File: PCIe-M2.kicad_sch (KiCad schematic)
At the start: 24 parts, among them J4 Bus_M.2_Socket_M, M1 M.2 Screw, M2 M.2 Solder Nut, M3 M.2 Solder Nut, M4 M.2 Solder Nut, M5 M.2 Solder Nut, U7 ASEK-32.768KHZ-L-R-T, U8 AP3441SHE-7B

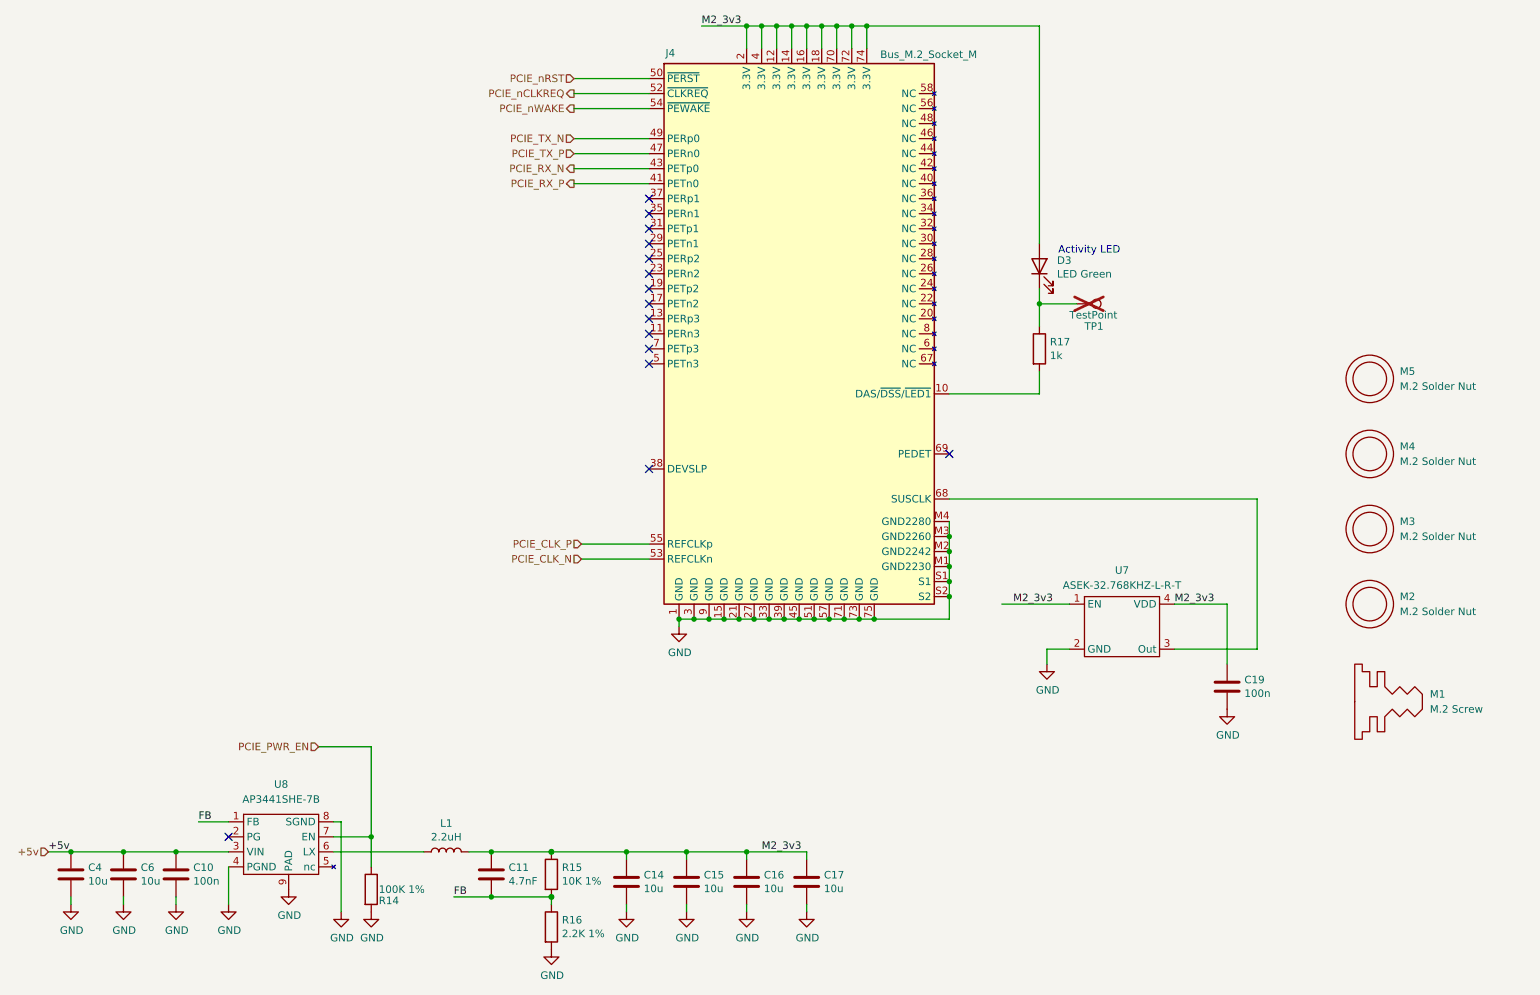
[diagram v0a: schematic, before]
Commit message: voltage regulator refactoring
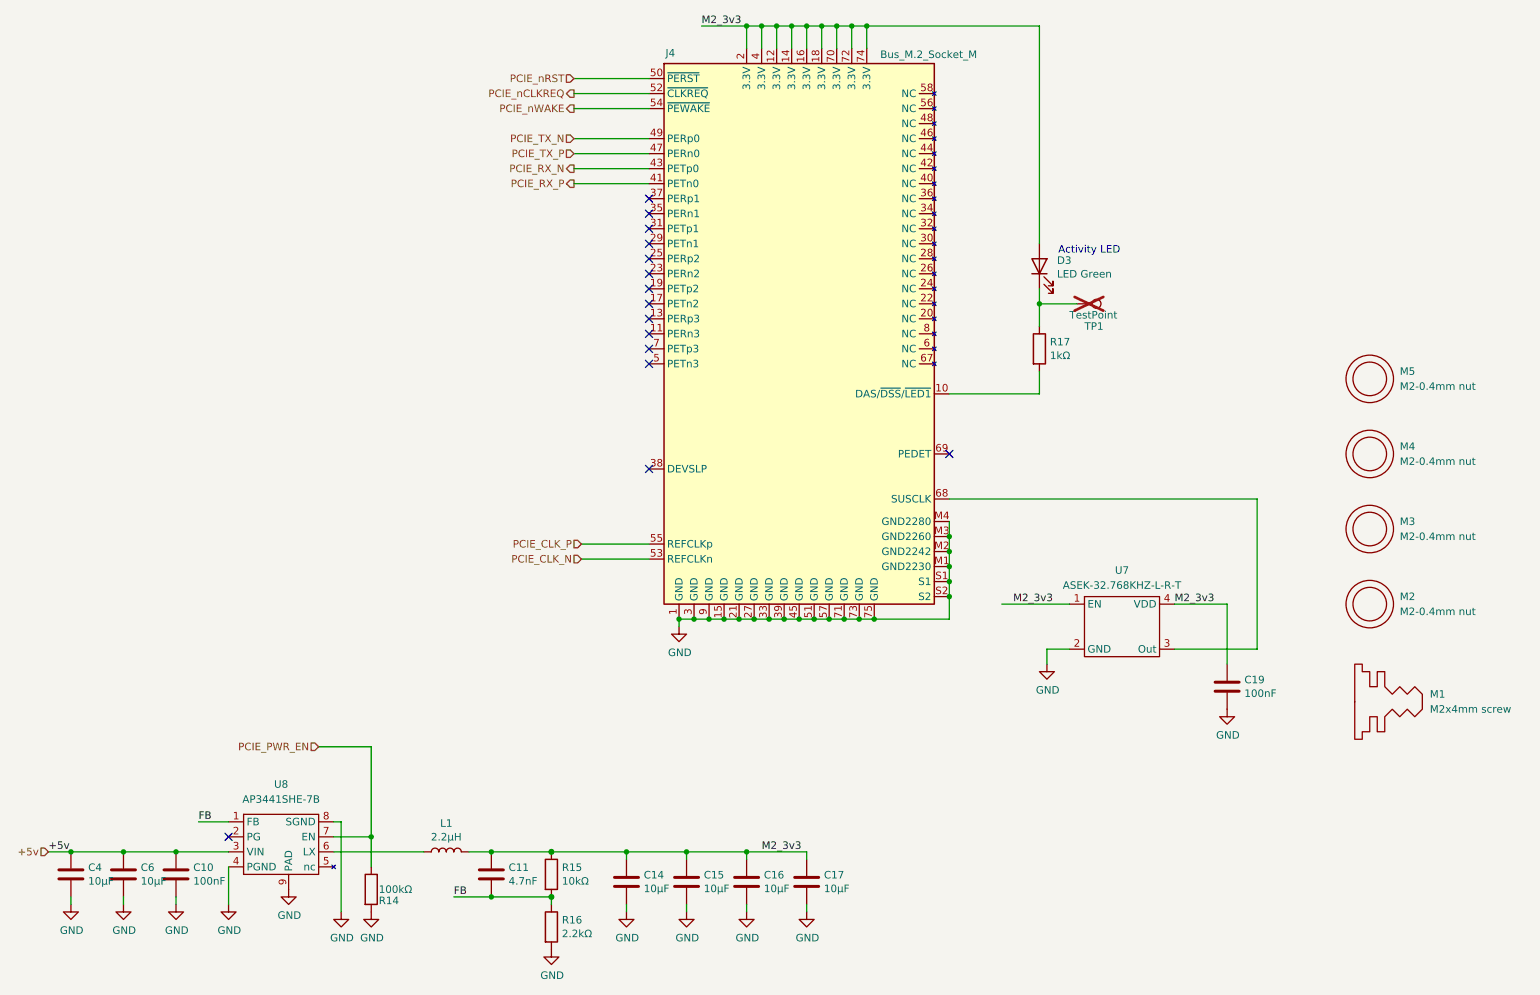
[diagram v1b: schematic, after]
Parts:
- C10, C19: value 100n -> 100nF; Dist. P/N (none) -> 478-11504-2-ND; Distributor (none) -> Digikey; Field4 Farnell -> (none); Field5 2611911 -> (none); Field6 RM EMK105 B7104KV-F -> (none); Field7 TAIYO YUDEN EUROPE GMBH -> (none); Field8 110091611 -> (none); Manf. P/N (none) -> 04026D104KAT4A; Manufacturer (none) -> Kyocera; Part Description 0.1uF 10% 16V Ceramic Capacitor X7R 0402 (1005 Metric) -> Capacitor, Ceramic, 0.1µF, ±10%, 6.3V, X5R, 0402 (1005m)
- C11: Dist. P/N (none) -> 478-KGM05AR71A472KHTR-ND; Distributor (none) -> Digikey; Manf. P/N (none) -> KGM05AR71A472KH; Manufacturer (none) -> Kyocera; Part Description 4.7nF capacitor 0402 -> Capacitor, Ceramic, 4700pF, ±10%, 10V, X7R, 0402 (1005m)
- C14, C15, C16, C17, C4, C6: value 10u -> 10µF; Dist. P/N (none) -> 478-KGM21AR51A106KUTR-ND; Distributor (none) -> Digikey; Field4 Digikey -> (none); Field5 490-14381-1-ND -> (none); Field6 GRM21BR71A106KA73L -> (none); Field7 Murata -> (none); Field8 111893011 -> (none); Manf. P/N (none) -> 0805ZD106KAT2A; Manufacturer (none) -> Kyocera; Part Description 10uF 10% 10V Ceramic Capacitor X7R 0805 (2012 Metric) -> Capacitor, Ceramic, 10µF, ±10%, 10V, X5R, 0805 (2012m)
- D3: Dist. P/N (none) -> 160-1478-2-ND; Distributor (none) -> Digikey; Field4 Digikey -> (none); Field5 LTST-S270KGKT -> (none); Field6 SML-A12M8TT86N -> (none); Field7 Rohm -> (none); Manf. P/N (none) -> LTST-S270KGKT; Manufacturer (none) -> Lite-On Inc.; Part Description Green 572nm LED Indication - Discrete 2.2V 2-SMD, No Lead -> LED, Green, 572nm, 2.2V, SMD 0603
- J4: Dist. P/N (none) -> A115902TR-ND; Distributor (none) -> Digikey; Field5 MTSSD03-67MSW337 -> (none); Field6 MTSSD03-67MSW337 -> (none); Field7 MTCONN -> (none); Manf. P/N (none) -> 1-2199119-5; Manufacturer (none) -> TE Connectivity; Part Description M.2 M Key connector -> Connector, M.2, M-Key, 67 pin, 0.5mm P, 3.2mm H
- L1: value 2.2uH -> 2.2µH; Dist. P/N (none) -> 118-SRP5030CC-2R2MTR-ND; Distributor (none) -> Digikey; Field5 SRP5030CC-2R2M -> (none); Field6 SRP5030CC-2R2M -> (none); Field7 Bourns -> (none); Manf. P/N (none) -> SRP5030CC-2R2M; Manufacturer (none) -> Bourns; Part Description Inductor, SMT, 2520, 2u2, IRMS=7A, ISAT=8A, DCR=0.032R -> Inductor, 2.2µH, ±20%, 7A, 32Ω
- M1: value M.2 Screw -> M2x4mm screw; Dist. P/N (none) -> 92000A011; Distributor (none) -> McMaster; Manf. P/N (none) -> N/A; Manufacturer (none) -> Misc.; Part Description M.2 Screw -> PHCS, M2-0.4 x 4mm, Phillips, Stainless Steel
- M2, M3, M4, M5: value M.2 Solder Nut -> M2-0.4mm nut; Dist. P/N (none) -> C2916320; Distributor (none) -> LCSC; Manf. P/N (none) -> SMTSO2015CTJ; Manufacturer (none) -> Sinhoo; Part Description Solder nut for M.2 slot -> Standoff, M2 thread, 1.5mm H, 5.56mm Diam.
- R14: value 100K 1% -> 100kΩ; Dist. P/N (none) -> 10-ERJ-U02F1003XTR-ND; Distributor (none) -> Digikey; Field4 Farnell -> (none); Field6 MCR01MZPF1003 -> (none); Field7 Rohm -> (none); Manf. P/N (none) -> ERJ-U02F1003X; Manufacturer (none) -> Panasonic; Part Description Resistor 100K M1005 1% 63mW -> Resistor, 100kΩ, ±1%, 0.1W, SMD 0402 (1005m)
- R15: value 10K 1% -> 10kΩ; Dist. P/N (none) -> 10-ERJ-U02F1002XTR-ND; Distributor (none) -> Digikey; Field4 Farnell -> (none); Field6 MCR01MZPF1002 -> (none); Field7 Rohm -> (none); Manf. P/N (none) -> ERJ-U02F1002X; Manufacturer (none) -> Panasonic; Part Description Resistor 10K M1005 1% 63mW -> Resistor, 10kΩ, ±1%, 0.1W, SMD 0402 (1005m)
- R16: value 2.2K 1% -> 2.2kΩ; Dist. P/N (none) -> P2.20KLTR-ND; Distributor (none) -> Digikey; Field4 Farnell -> (none); Manf. P/N (none) -> ERJ-2RKF2201X; Manufacturer (none) -> Panasonic; Part Description Resistor 2.2K M1005 1% 63mW -> Resistor, 2.2kΩ, ±1%, 0.1W, SMD 0402 (1005m)
- R17: value 1k -> 1kΩ; Dist. P/N (none) -> 10-ERJ-H2RF1001XTR-ND; Distributor (none) -> Digikey; Field4 Farnell -> (none); Field5 9239235 -> (none); Field6 RK73H1ETTP1001F -> (none); Field7 KOA EUROPE GMBH -> (none); Field8 125049511 -> (none); Manf. P/N (none) -> ERJ-H2RF1001X; Manufacturer (none) -> Panasonic; Part Description Resistor 1K M1005 1% 63mW -> Resistor, 1kΩ, ±1%, 0.1W, SMD 0402 (1005m)
- TP1: Dist. P/N (none) -> nf; Distributor (none) -> nf; Field4 nf -> (none); Field5 nf -> (none); Field6 nf -> (none); Field7 nf -> (none)
- U7: Dist. P/N (none) -> 535-ASEK-32.768KHZ-L-R-TTR-ND; Distributor (none) -> Digikey; Field5 ASEK-32.768KHZ-L-R-T -> (none); Field6 ASEK-32.768KHZ-L-R-T -> (none); Field7 abracon -> (none); Manf. P/N (none) -> ASEK-32.768KHZ-L-R-T; Manufacturer (none) -> Abracon; Part Description 32KHz Xtal oscilator -> Oscillator, 32.768kHz, 3.3V
- U8: Dist. P/N (none) -> AP3441SHE-7BDITR-ND; Distributor (none) -> Digikey; Field5 AP3441SHE-7B -> (none); Field6 AP3441SHE-7B -> (none); Field7 Diodes -> (none); Manf. P/N (none) -> AP3441SHE-7B; Manufacturer (none) -> Diodes Inc.; Part Description 3A DC-DC converter -> Buck Converter, 0.6V, 3A

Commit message: fix all DRC issues
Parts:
- TP1: footprint TestPoint:TestPoint_Pad_2.0x2.0mm -> TestPoint:TestPoint_Pad_D1.5mm
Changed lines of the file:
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@@
 			)
 		)
-		(property "Footprint" "TestPoint:TestPoint_Pad_2.0x2.0mm"
+		(property "Footprint" "TestPoint:TestPoint_Pad_D1.5mm"
 			(at 208.28 80.01 0)
 			(effects

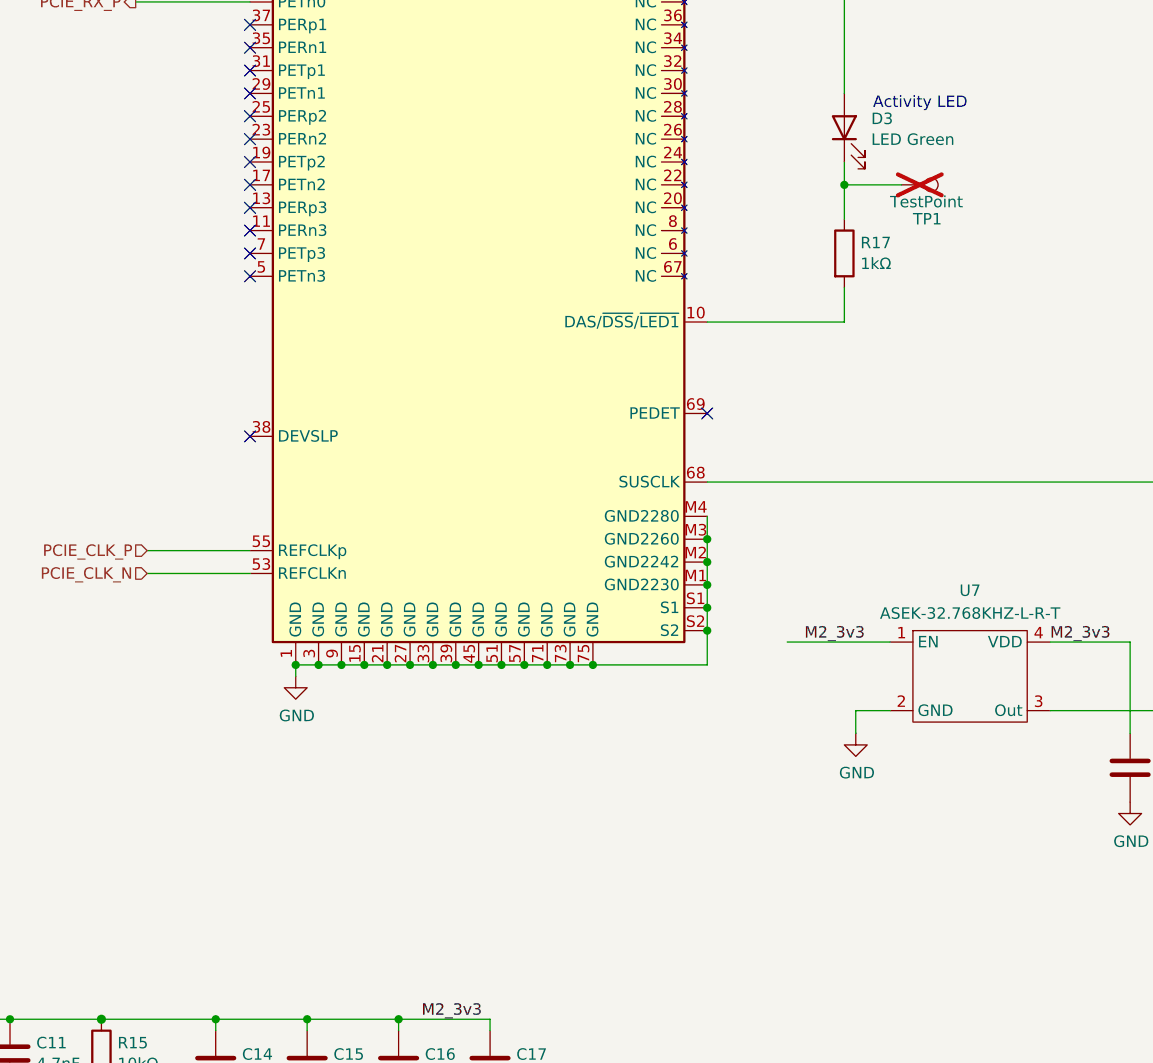
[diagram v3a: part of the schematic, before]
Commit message: final review, added coincell back, additional testpoints, updated i2c bus for quic
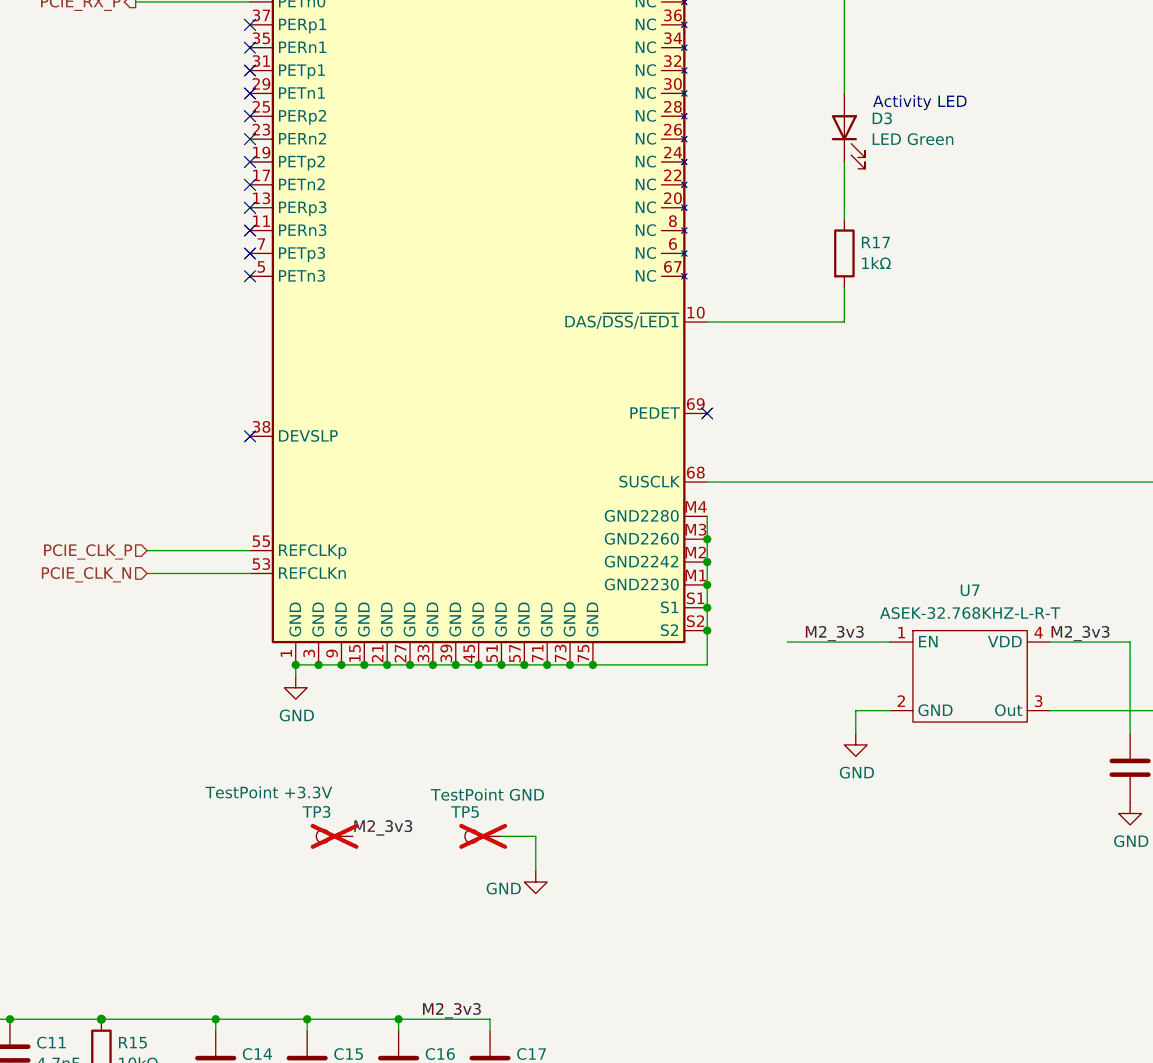
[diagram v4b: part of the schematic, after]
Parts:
- removed TP1: TestPoint, TestPoint:TestPoint_Pad_D1.5mm, symbol Connector:TestPoint
- added TP3: TestPoint +3.3V, TestPoint:TestPoint_Pad_D1.5mm, symbol Connector:TestPoint
- added TP5: TestPoint GND, TestPoint:TestPoint_Pad_D1.5mm, symbol Connector:TestPoint
- J4: footprint CM5IO:M.2 M Key socket -> libreboard:M.2 M Key socket
- L1: footprint CM5IO:L_Bourns_SRP5030CC -> libreboard:L_Bourns_SRP5030CC
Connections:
- net GND: now also TP5.1
- net M2_3v3: now also TP3.1
